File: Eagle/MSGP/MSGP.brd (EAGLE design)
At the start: 71.8 x 43.9 mm, 18 parts, among them IC1 74ALS04D, IC2 NE5532D, U1 LTC6905CS5TRMPBF

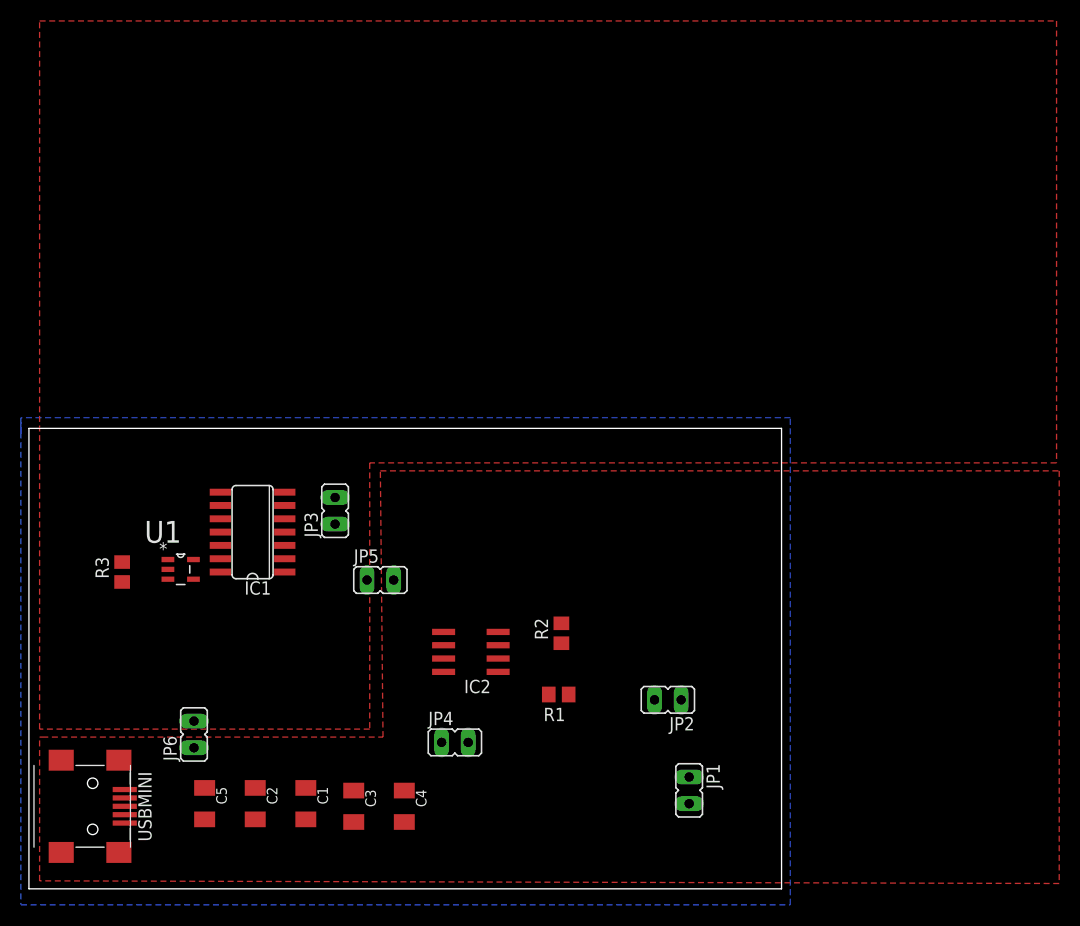
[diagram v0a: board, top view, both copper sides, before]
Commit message: fixed polygon
Because Eagle is dumb….
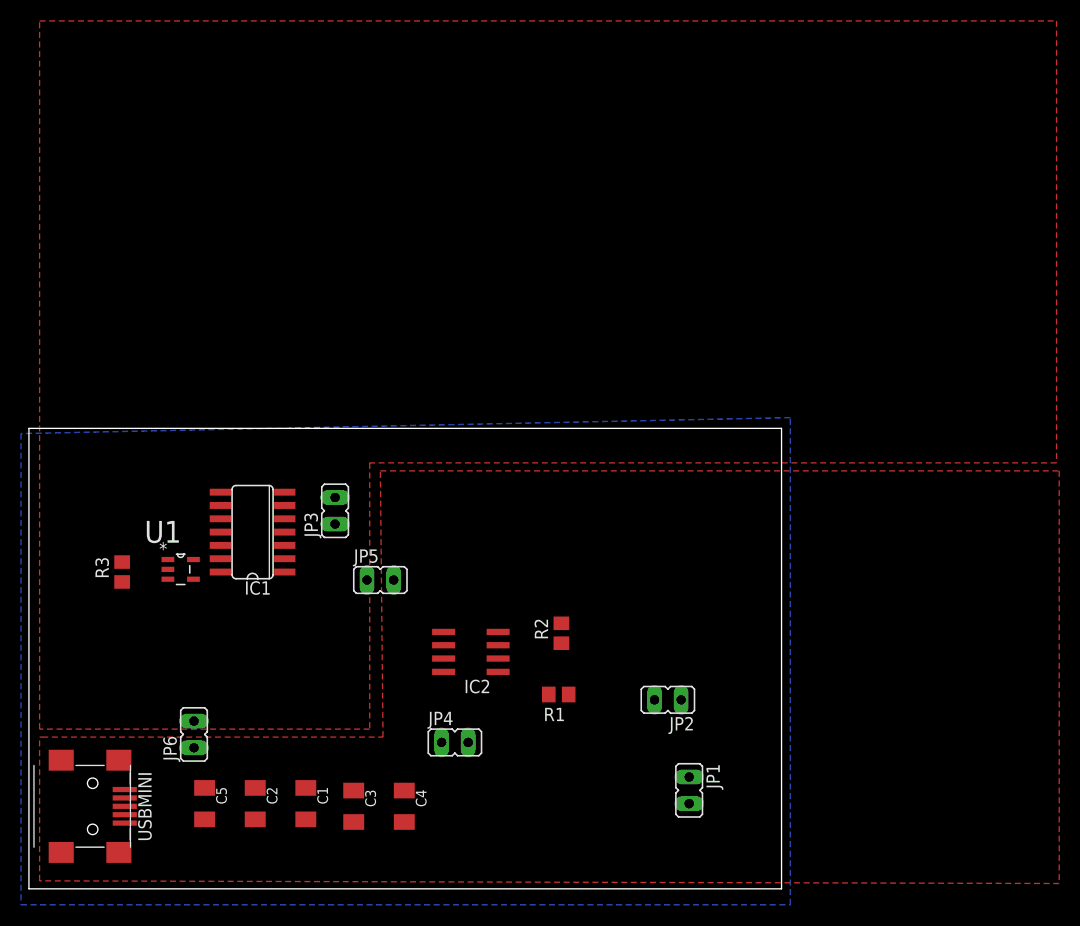
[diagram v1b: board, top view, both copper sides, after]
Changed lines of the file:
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@@
 <?xml version="1.0" encoding="utf-8"?>
 <!DOCTYPE eagle SYSTEM "eagle.dtd">
-<eagle version="7.1.0">
+<eagle version="7.2.0">
 <drawing>
 <settings>
@@
 <contactref element="C2" pad="2"/>
 <contactref element="JP4" pad="2"/>
-<polygon width="0.4064" layer="16">
-<vertex x="-0.762" y="44.45"/>
+<polygon width="0.4064" layer="16" rank="4">
 <vertex x="-0.762" y="-1.524"/>
 <vertex x="72.644" y="-1.524"/>
 <vertex x="72.644" y="44.958"/>
-<vertex x="-0.762" y="44.958"/>
 <vertex x="-0.762" y="43.434"/>
 </polygon>
@@
 <contactref element="JP6" pad="1"/>
 <contactref element="JP6" pad="2"/>
-<wire x1="62.992" y1="8.128" x2="62.23" y2="18.034" width="0" layer="19" extent="1-1"/>
-<wire x1="44.764" y1="23.241" x2="62.23" y2="18.034" width="0" layer="19" extent="1-1"/>
-<wire x1="44.764" y1="24.511" x2="44.764" y2="23.241" width="0" layer="19" extent="1-1"/>
-<wire x1="41.91" y1="13.97" x2="44.764" y2="23.241" width="0" layer="19" extent="1-1"/>
-<wire x1="35.814" y1="6.374" x2="41.91" y2="13.97" width="0" layer="19" extent="1-1"/>
-<wire x1="30.988" y1="6.374" x2="35.814" y2="6.374" width="0" layer="19" extent="1-1"/>
-<wire x1="21.59" y1="6.628" x2="30.988" y2="6.374" width="0" layer="19" extent="1-1"/>
-<wire x1="16.764" y1="6.628" x2="21.59" y2="6.628" width="0" layer="19" extent="1-1"/>
-<wire x1="9.144" y1="6.274" x2="16.764" y2="6.628" width="0" layer="19" extent="1-1"/>
-<wire x1="29.21" y1="37.338" x2="44.764" y2="24.511" width="0" layer="19" extent="1-1"/>
-<wire x1="24.4094" y1="37.846" x2="29.21" y2="37.338" width="0" layer="19" extent="1-1"/>
-<wire x1="34.798" y1="29.464" x2="9.144" y2="6.274" width="0" layer="19" extent="1-1"/>
-<wire x1="32.258" y1="29.464" x2="34.798" y2="29.464" width="0" layer="19" extent="1-1"/>
-<wire x1="15.748" y1="13.462" x2="32.258" y2="29.464" width="0" layer="19" extent="1-1"/>
-<wire x1="15.748" y1="16.002" x2="15.748" y2="13.462" width="0" layer="19" extent="1-1"/>
 </signal>
 <signal name="VCC">
@@
 <wire x1="16.764" y1="9.628" x2="21.59" y2="9.628" width="0" layer="19" extent="1-1"/>
 <wire x1="9.144" y1="9.474" x2="16.764" y2="9.628" width="0" layer="19" extent="1-1"/>
-<wire x1="8.89" y1="31.176" x2="9.144" y2="9.474" width="0" layer="19" extent="1-1"/>
-<wire x1="13.2588" y1="31.4198" x2="8.89" y2="31.176" width="0" layer="19" extent="1-1"/>
-<wire x1="15.6972" y1="29.5402" x2="13.2588" y2="31.4198" width="0" layer="19" extent="1-1"/>
+<wire x1="15.6972" y1="29.5402" x2="16.764" y2="9.628" width="0" layer="19" extent="1-1"/>
 <wire x1="18.2626" y1="30.226" x2="15.6972" y2="29.5402" width="0" layer="19" extent="1-1"/>
+<wire x1="13.2588" y1="31.4198" x2="15.6972" y2="29.5402" width="0" layer="19" extent="1-1"/>
+<wire x1="8.89" y1="31.176" x2="13.2588" y2="31.4198" width="0" layer="19" extent="1-1"/>
 </signal>
 <signal name="N$4">
